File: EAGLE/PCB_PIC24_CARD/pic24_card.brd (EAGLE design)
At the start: 24 x 60 mm, 25 parts, among them IC1 PIC24FJ256GL410, IC2 XR3072XID-F, M1 MOUNTING_3M_3.2MM, X1 CONN_SMD_67P-P0.5-V_NASB0-S67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, X2 M.2_MKEY_FINGERS, X3 5-PIN_2.54_HEADER

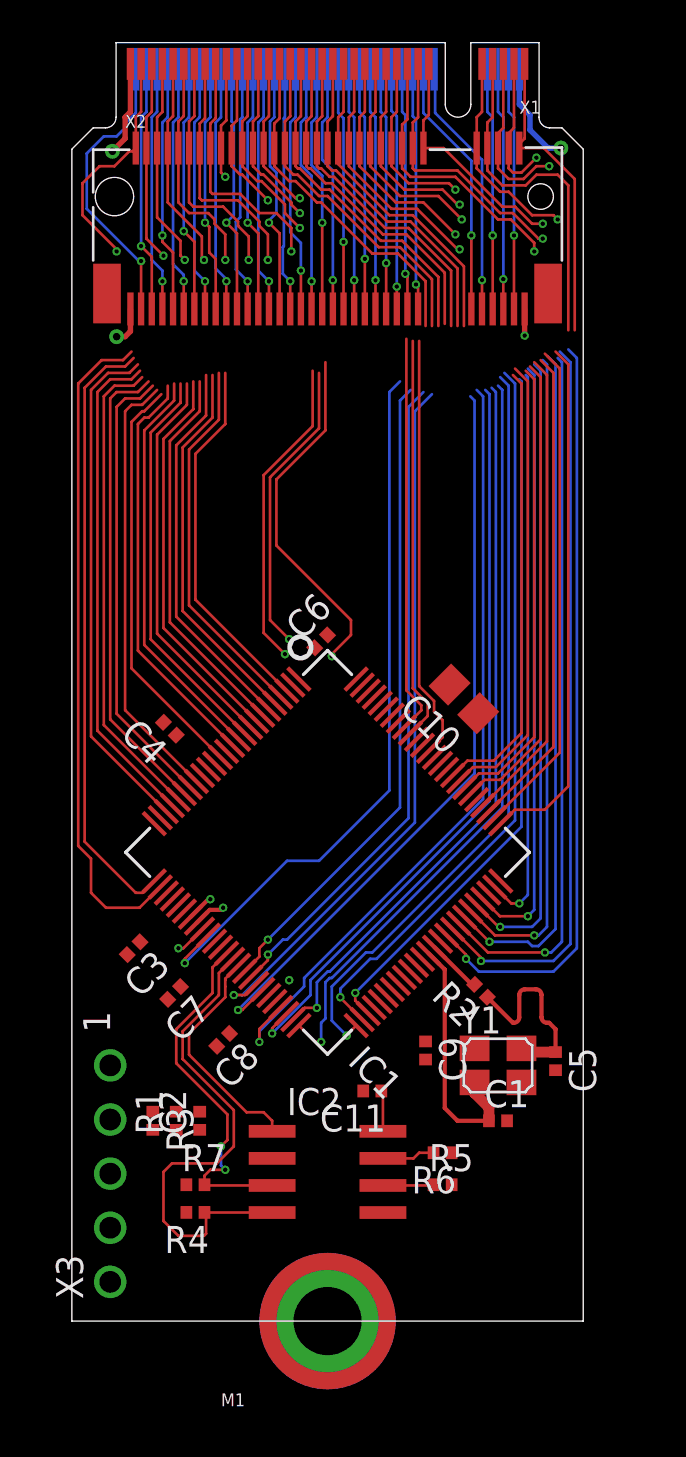
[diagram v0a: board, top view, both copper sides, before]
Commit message: finished breaking out pic pins up near connector
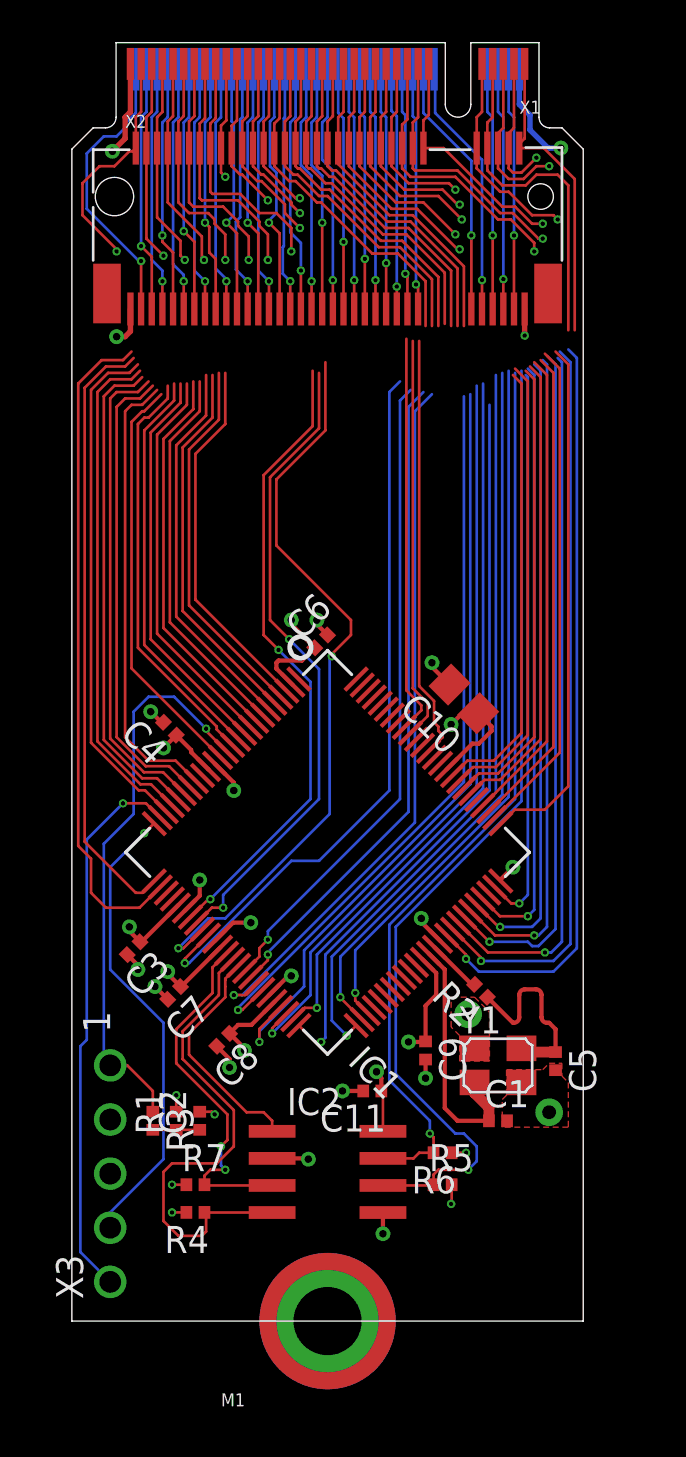
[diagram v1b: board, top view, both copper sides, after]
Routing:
- net A: track 2.39 -> 46.5 mm, vias 0 -> 1
- net B: track 2.48 -> 42.4 mm, vias 0 -> 1
- net +3V3: track 8.04 -> 41.1 mm, vias 2 -> 13
- net MCLR: track 0.00 -> 26.5 mm, vias 0 -> 1
- net PGC: track 0.00 -> 25.9 mm, vias 0 -> 1
- net GND: track 6.26 -> 28.2 mm, vias 3 -> 23
- net PGD: track 0.00 -> 21.9 mm, vias 0 -> 1
- net N$66: track 0.00 -> 2.20 mm
- net N$74: track 35.8 -> 34.5 mm
- net N$93: track 20.7 -> 21.4 mm
- net N$120: track 21.4 -> 22.1 mm
- net N$76: track 34.6 -> 33.9 mm
- net N$95: track 37.1 -> 36.5 mm
- net N$104: track 22.1 -> 22.6 mm
- added copper zone on layer 1, net GND

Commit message: pic24 card is done, gerbers and jlc files generated
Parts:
- added R8: 470R, _NIBE_rcl:R0402_NIBE
- added STATUS: LED_YELLOW, _NIBE_rcl:R0603
- moved C6 0.73 mm to (11.9, 32.6)
- moved C10 0.50 mm to (18.1, 29.6)
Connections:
- removed net N$10: X1.P$59, X2.16
- removed net N$100: IC1.88
- removed net N$101: IC1.23
- removed net N$102: IC1.22
- removed net N$103: IC1.21
- removed net N$104: IC1.20
- removed net N$105: IC1.26
- removed net N$106: IC1.27
- removed net N$107: IC1.32
- removed net N$108: IC1.33
- removed net N$109: IC1.34
- removed net N$11: X1.P$57, X2.18
- removed net N$110: IC1.35
- removed net N$111: IC1.41
- removed net N$112: IC1.42
- removed net N$113: IC1.43
- removed net N$114: IC1.44
- removed net N$115: IC1.9
- removed net N$116: IC1.10
- removed net N$117: IC1.11
- removed net N$118: IC1.12
- removed net N$119: IC1.14
- removed net N$12: X1.P$55, X2.20
- removed net N$120: IC1.19
- removed net N$121: IC1.91
- removed net N$122: IC1.92
- removed net N$13: X1.P$53, X2.22
- removed net N$14: X1.P$51, X2.24
- removed net N$15: X1.P$21, X2.54
- removed net N$16: X1.P$27, X2.48
- removed net N$17: X1.P$29, X2.46
- removed net N$18: X1.P$31, X2.44
- removed net N$19: X1.P$33, X2.42
- removed net N$2: X1.P$25, X2.50
- removed net N$20: X1.P$35, X2.40
- removed net N$21: X1.P$37, X2.38
- removed net N$22: X1.P$39, X2.36
- removed net N$23: X1.P$41, X2.34
- removed net N$24: X1.P$43, X2.32
- removed net N$25: X1.P$45, X2.30
- removed net N$26: X1.P$47, X2.28
- removed net N$27: X1.P$49, X2.26
- removed net N$28: X1.P$11, X2.56
- removed net N$29: X1.P$9, X2.58
- removed net N$3: X1.P$73, X2.2
- removed net N$33: X1.P$2, X2.75
- removed net N$34: X1.P$22, X2.55
- removed net N$35: X1.P$4, X2.73
- removed net N$4: X1.P$71, X2.4
- removed net N$40: X1.P$24, X2.53
- removed net N$41: X1.P$26, X2.51
- removed net N$42: X1.P$28, X2.49
- removed net N$43: X1.P$30, X2.47
- removed net N$44: X1.P$32, X2.45
- removed net N$45: X1.P$34, X2.43
- removed net N$46: X1.P$36, X2.41
- removed net N$47: X1.P$38, X2.39
- removed net N$48: X1.P$40, X2.37
- removed net N$49: X1.P$42, X2.35
- removed net N$5: X1.P$69, X2.6
- removed net N$50: X1.P$44, X2.33
- removed net N$51: X1.P$74, X2.3
- removed net N$52: X1.P$72, X2.5
- removed net N$53: X1.P$70, X2.7
- removed net N$54: X1.P$68, X2.9
- removed net N$55: X1.P$66, X2.11
- removed net N$56: X1.P$64, X2.13
- removed net N$57: X1.P$62, X2.15
- removed net N$58: X1.P$60, X2.17
- removed net N$59: X1.P$58, X2.19
- removed net N$6: X1.P$67, X2.8
- removed net N$60: X1.P$56, X2.21
- removed net N$61: X1.P$54, X2.23
- removed net N$62: X1.P$52, X2.25
- removed net N$63: X1.P$46, X2.31
- removed net N$64: X1.P$48, X2.29
- removed net N$65: X1.P$50, X2.27
- removed net N$68: IC1.3
- removed net N$69: IC1.4
- removed net N$7: X1.P$65, X2.10
- removed net N$70: IC1.5
- removed net N$72: IC1.48
- removed net N$73: IC1.49
- removed net N$74: IC1.50
- removed net N$75: IC1.51
- removed net N$76: IC1.52
- removed net N$77: IC1.53
- removed net N$78: IC1.68
- removed net N$79: IC1.69
- removed net N$8: X1.P$63, X2.12
- removed net N$80: IC1.70
- removed net N$81: IC1.71
- removed net N$82: IC1.72
- removed net N$83: IC1.77
- removed net N$84: IC1.76
- removed net N$85: IC1.78
- removed net N$86: IC1.81
- removed net N$87: IC1.82
- removed net N$88: IC1.83
- removed net N$89: IC1.84
- removed net N$9: X1.P$61, X2.14
- removed net N$90: IC1.6
- removed net N$91: IC1.7
- removed net N$92: IC1.8
- removed net N$93: IC1.18
- removed net N$95: IC1.47
- removed net N$96: IC1.66
- removed net N$97: IC1.67
- removed net N$98: IC1.74
- removed net N$99: IC1.79
- new net AN10: IC1.34, X1.P$47, X2.28
- new net AN11: IC1.35, X1.P$58, X2.19
- new net AN12: IC1.41, X1.P$45, X2.30
- new net AN13: IC1.42, X1.P$43, X2.32
- new net AN14: IC1.43, X1.P$56, X2.21
- new net AN15: IC1.44, X1.P$50, X2.27
- new net AN16: IC1.9, X1.P$57, X2.18
- new net AN17: IC1.10, X1.P$64, X2.13
- new net AN18: IC1.11, X1.P$59, X2.16
- new net AN19: IC1.12, X1.P$61, X2.14
- new net AN2: IC1.23, X1.P$70, X2.7
- new net AN20: IC1.14, X1.P$66, X2.11
- new net AN21: IC1.19, X1.P$65, X2.10
- new net AN22: IC1.91, X1.P$52, X2.25
- new net AN23: IC1.92, X1.P$54, X2.23
- new net AN3: IC1.22, X1.P$69, X2.6
- new net AN4: IC1.21, X1.P$67, X2.8
- new net AN5: IC1.20, X1.P$68, X2.9
- new net AN6: IC1.26, X1.P$71, X2.4
- new net AN7: IC1.27, X1.P$72, X2.5
- new net AN8: IC1.32, X1.P$60, X2.17
- new net AN9: IC1.33, X1.P$49, X2.26
- new net LED_STATUS: IC1.54, R8.1
- new net RC13: IC1.73, X1.P$22, X2.55
- new net RP10: IC1.49, X1.P$35, X2.40
- new net RP11: IC1.72, X1.P$36, X2.41
- new net RP12: IC1.71, X1.P$34, X2.43
- new net RP15: IC1.53, X1.P$27, X2.48
- new net RP16: IC1.51, X1.P$31, X2.44
- new net RP17: IC1.50, X1.P$33, X2.42
- new net RP2: IC1.68, X1.P$28, X2.49
- new net RP20: IC1.82, X1.P$21, X2.54
- new net RP22: IC1.78, X1.P$44, X2.33
- new net RP23: IC1.77, X1.P$42, X2.35
- new net RP24: IC1.76, X1.P$40, X2.37
- new net RP25: IC1.81, X1.P$48, X2.29
- new net RP3: IC1.70, X1.P$32, X2.45
- new net RP30: IC1.52, X1.P$29, X2.46
- new net RP32: IC1.83, X1.P$23, X2.52
- new net RP33: IC1.84, X1.P$25, X2.50
- new net RP34: IC1.3, X1.P$51, X2.24
- new net RP35: IC1.4, X1.P$73, X2.2
- new net RP36: IC1.5, X1.P$74, X2.3
- new net RP4: IC1.69, X1.P$30, X2.47
- new net RP5: IC1.48, X1.P$37, X2.38
- new net RPI37: IC1.74, X1.P$38, X2.39
- new net RPI38: IC1.6, X1.P$53, X2.22
- new net RPI39: IC1.7, X1.P$62, X2.15
- new net RPI40: IC1.8, X1.P$55, X2.20
- new net RPI42: IC1.79, X1.P$46, X2.31
- new net RPI43: IC1.47, X1.P$39, X2.36
- new net RPI45: IC1.88, X1.P$41, X2.34
- new net RPI47: IC1.18, X1.P$63, X2.12
- new net RPI49: IC1.67, X1.P$26, X2.51
- new net RPI50: IC1.66, X1.P$24, X2.53
- net A: now also X1.P$9, X2.58
- net B: now also X1.P$11, X2.56
- net GND: now also STATUS.1, X1.P$2, X1.P$4, X2.73, X2.75
- net N$1: now also R8.2, STATUS.2; no longer X1.P$23, X2.52
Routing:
- net AN15: track 0.00 -> 56.2 mm, vias 0 -> 4
- net RPI43: track 0.00 -> 55.2 mm, vias 0 -> 3
- net RPI49: track 0.00 -> 54.1 mm, vias 0 -> 2
- net RP5: track 0.00 -> 53.9 mm, vias 0 -> 3
- net RP17: track 0.00 -> 53.4 mm, vias 0 -> 3
- net RPI50: track 0.00 -> 53.3 mm, vias 0 -> 2
- net RP2: track 0.00 -> 52.9 mm, vias 0 -> 2
- net RP16: track 0.00 -> 52.6 mm, vias 0 -> 3
- net AN14: track 0.00 -> 52.1 mm, vias 0 -> 4
- net RP4: track 0.00 -> 51.9 mm, vias 0 -> 2
- net RP30: track 0.00 -> 51.7 mm, vias 0 -> 3
- net RP10: track 0.00 -> 51.7 mm, vias 0 -> 3
- net AN11: track 0.00 -> 51.5 mm, vias 0 -> 4
- net RC13: track 0.00 -> 51.4 mm, vias 0 -> 2
- net RP15: track 0.00 -> 50.2 mm, vias 0 -> 3
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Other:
- board text added: "PIC STIC 1"
